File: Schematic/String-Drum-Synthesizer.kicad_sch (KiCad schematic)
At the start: 43 parts, among them J1 USB_B, J2 USB_A, J3 HDMI_A_1.4, U1 LM1117MP-3.3, U4 LM3900DR, U5 LM1117MP-3.3, U6 STM32F722RCTx

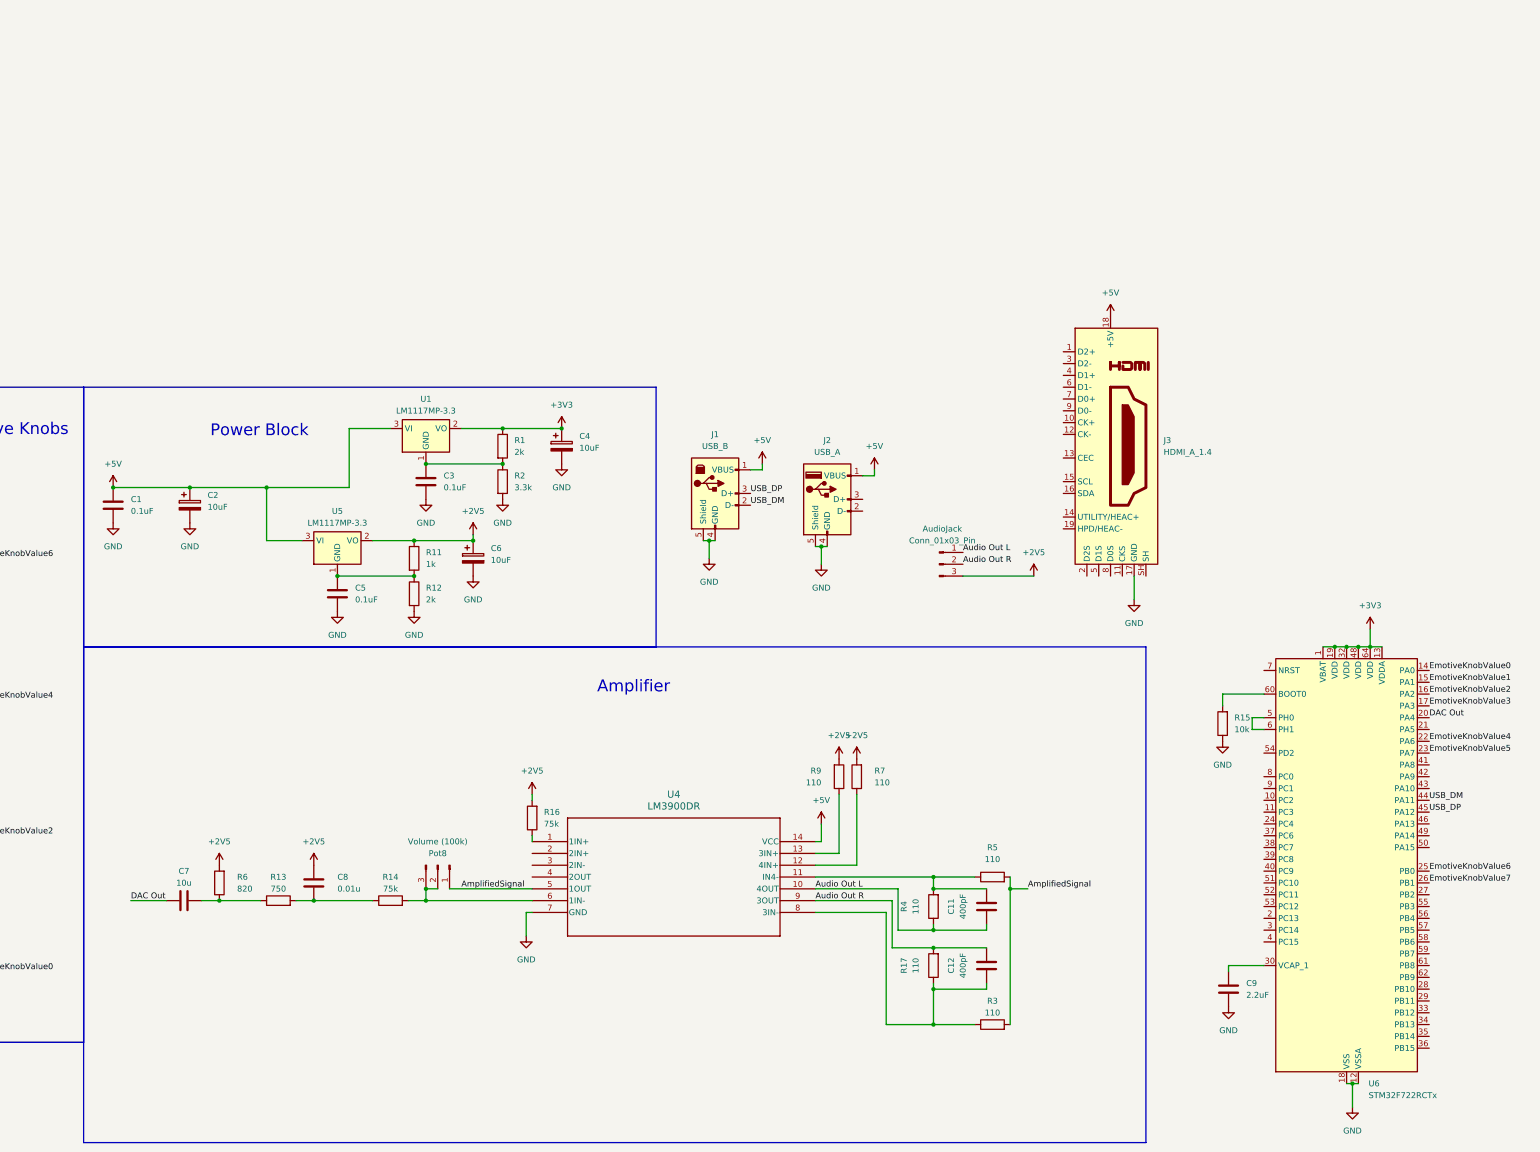
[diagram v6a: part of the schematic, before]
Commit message: Adding peripheral USB hardware
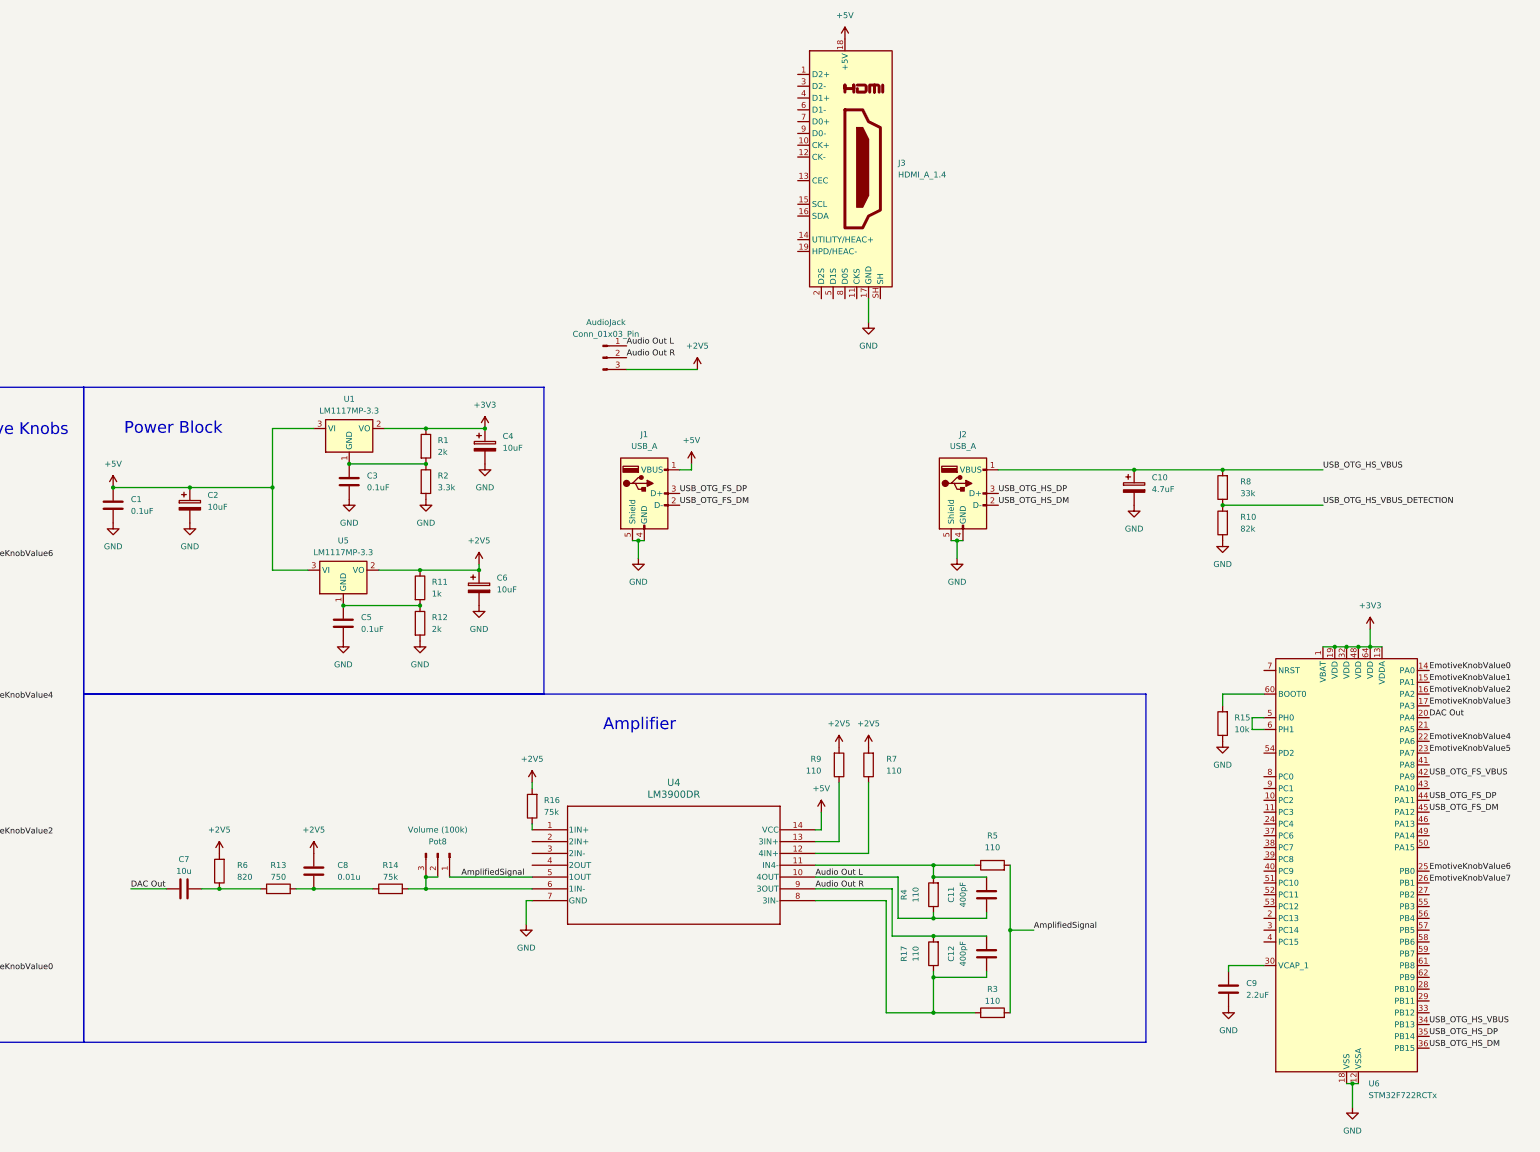
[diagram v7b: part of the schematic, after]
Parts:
- removed J1: USB_B, symbol Connector:USB_B
- added C10: 4.7uF, symbol Device:C_Polarized
- added J1: USB_A, symbol Connector:USB_A
- added R10: 82k, symbol Device:R
- added R8: 33k, symbol Device:R
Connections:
- net +5V: now also J1.1 (VBUS); no longer J2.1 (VBUS)
- net GND: now also C10.2, J1.4 (GND), J1.5 (Shield), R10.1
- net USB_OTG_HS_VBUS: now reaches U6.34 (PB13)
- net USB_OTG_HS_VBUS: now also J2.1 (VBUS), C10.1, R8.2
- net USB_OTG_HS_DP: now reaches U6.35 (PB14)
- net USB_OTG_HS_DP: now also J2.3 (D+)
- net USB_OTG_HS_DM: now reaches U6.36 (PB15)
- net USB_OTG_HS_DM: now also J2.2 (D-)
- net USB_OTG_FS_VBUS: now reaches U6.42 (PA9)
- net USB_DM renamed USB_OTG_FS_DP
- net USB_OTG_FS_DP: now also J1.3 (D+)
- net USB_DP renamed USB_OTG_FS_DM
- net USB_OTG_FS_DM: now also J1.2 (D-)
- new net USB_OTG_HS_VBUS_DETECTION: R10.2, R8.1
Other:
- moved on the sheet: AudioJack, C11, C12, C3, C4, C5, C6, C7, C8, J2, J3, Pot8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

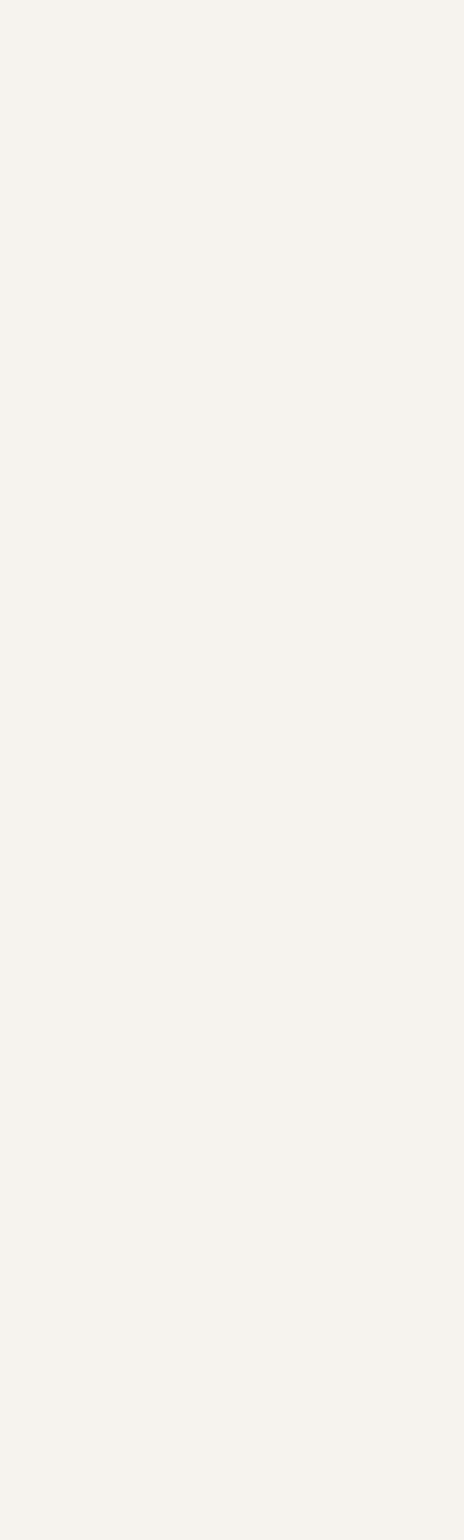
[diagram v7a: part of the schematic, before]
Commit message: Added HDMI Chip
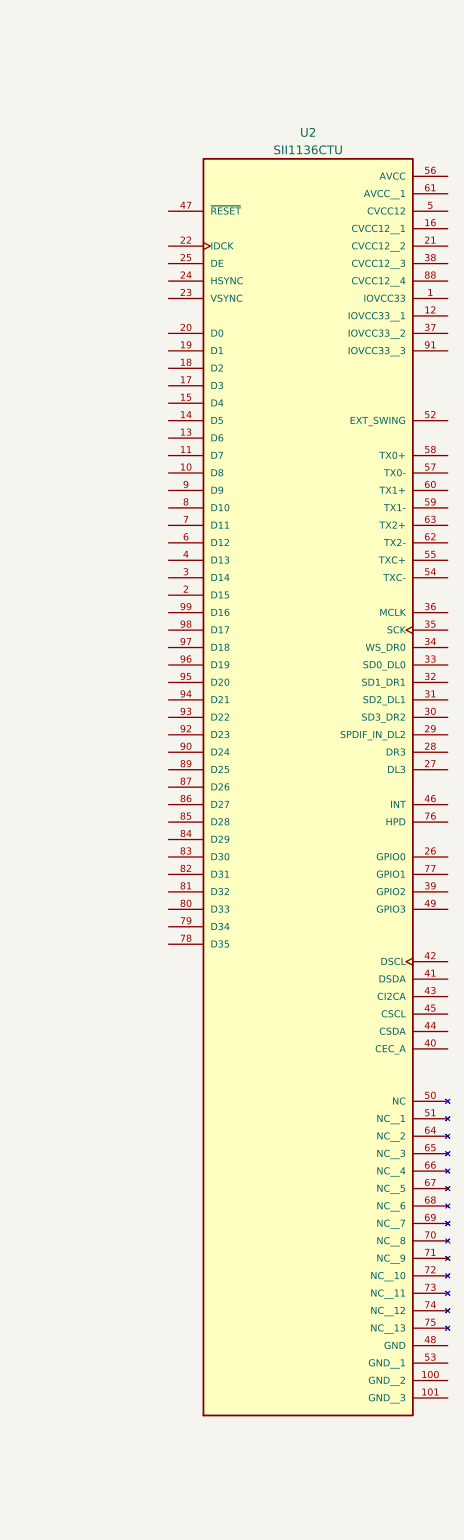
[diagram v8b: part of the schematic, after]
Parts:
- added U2: SII1136CTU, SII1136CTU:QFP50P1600X1600X120-101N, symbol SII1136CTU:SII1136CTU
